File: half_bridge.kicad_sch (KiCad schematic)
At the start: 2 parts, among them U1 74HC04, U2 74HC08

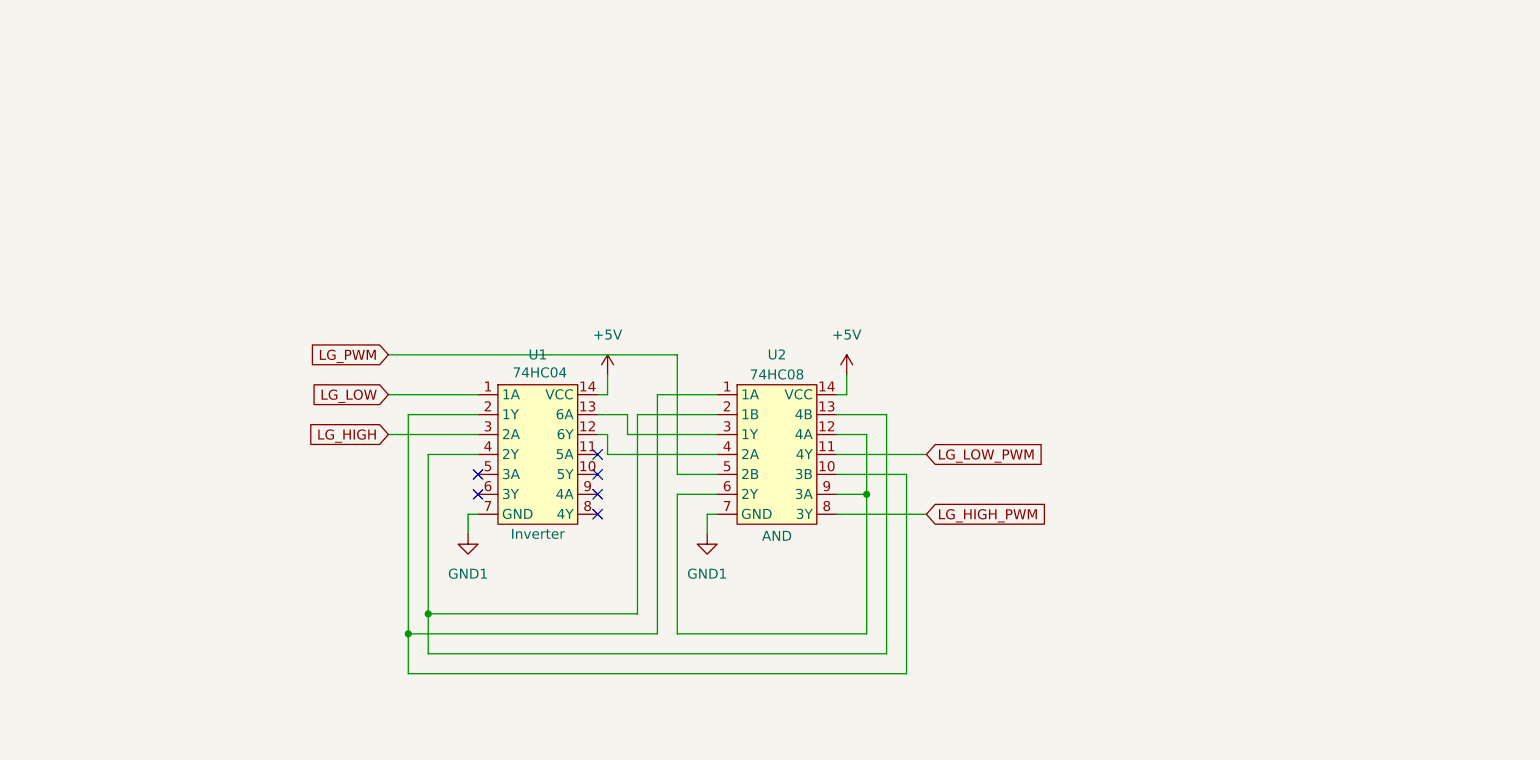
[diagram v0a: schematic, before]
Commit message: Added pwm optocoupler
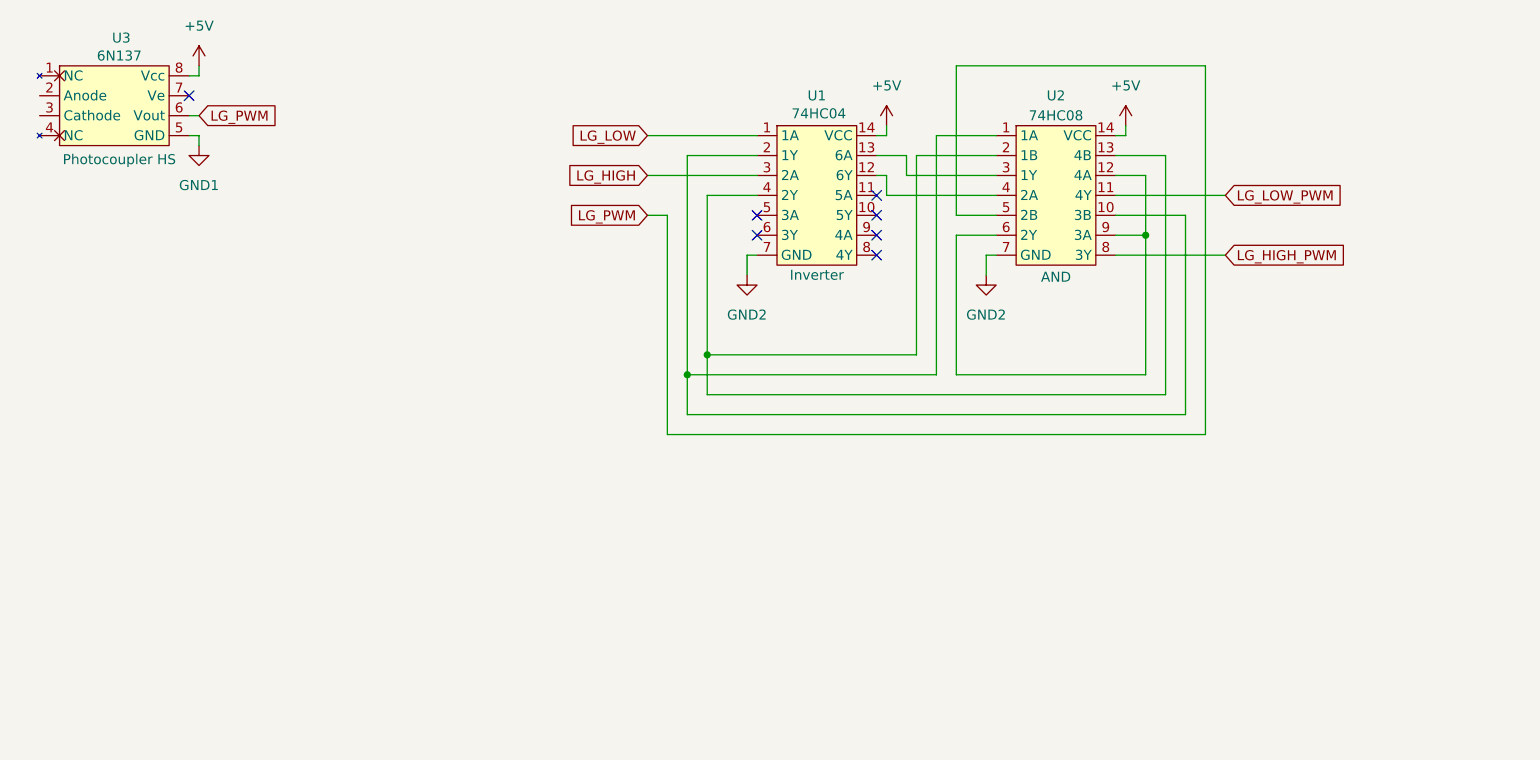
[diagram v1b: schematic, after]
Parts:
- added U3: 6N137, Package_SO:SOP-8_6.605x9.655mm_P2.54mm, symbol symbols:6N137
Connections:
- net +5V: now also U3.8 (Vcc)
- net GND1: now also U3.5 (GND); no longer U1.7 (GND), U2.7 (GND)
- net LG_PWM: now also U3.6 (Vout)
- new net GND2: U1.7 (GND), U2.7 (GND)
- no-connect marks 6 -> 7
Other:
- moved on the sheet: U1, U2

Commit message: Finished logic gates and optocoupler logical connections
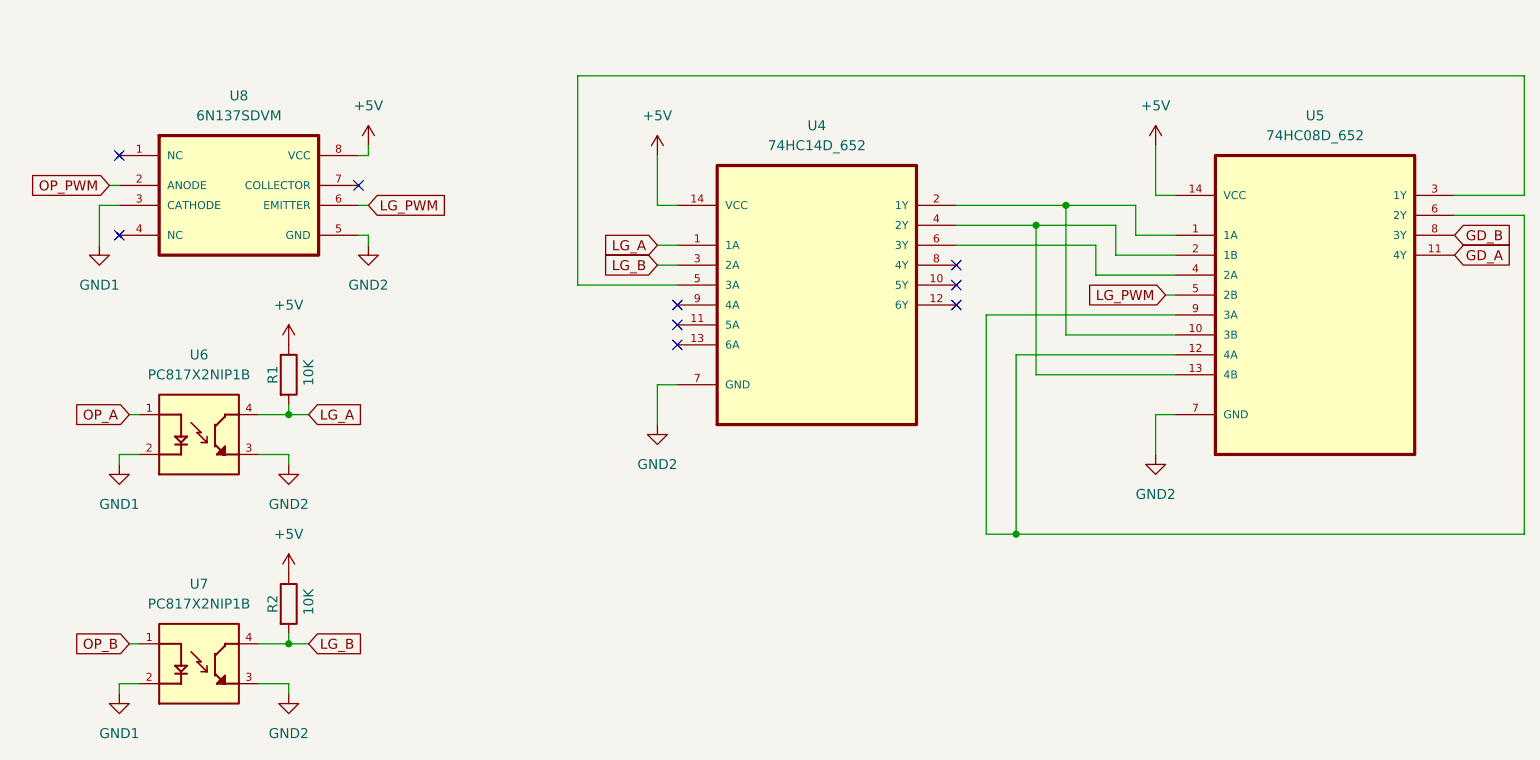
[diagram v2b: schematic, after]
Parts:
- removed U1: 74HC04, Package_SO:SOIC-14_3.9x8.7mm_P1.27mm, symbol symbols:74HC04
- removed U2: 74HC08, Package_SO:SOIC-14_3.9x8.7mm_P1.27mm, symbol symbols:74HC08
- removed U3: 6N137, Package_SO:SOP-8_6.605x9.655mm_P2.54mm, symbol symbols:6N137
- added R1, R2: 10K, footprints:R_0603_1608Metric_Pad0.98x0.95mm_HandSolder, symbol symbols:R_10K_Ohm
- added U4: 74HC14D_652, footprints:SOIC127P600X175-14N, symbol symbols:74HC14D_652
- added U5: 74HC08D_652, footprints:SOIC127P600X175-14N, symbol symbols:74HC08D_652
- added U6, U7: PC817X2NIP1B, footprints:SOIC254P960X420-4N, symbol symbols:PC817X2NIP1B
- added U8: 6N137SDVM, footprints:COUPL_6N138SDM, symbol symbols:6N137SDVM
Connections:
- net +5V: now also R1.1, R2.1, U4.14 (VCC), U5.14 (VCC), U8.8 (VCC)
- net GND1: now also U6.2, U7.2, U8.3 (CATHODE)
- net GND2: now also U4.7 (GND), U5.7 (GND), U6.3, U7.3, U8.5 (GND)
- net LG_PWM: now also U5.5 (2B), U8.6 (EMITTER)
- new net: U4.2 (1Y), U5.1 (1A), U5.10 (3B)
- new net: U4.4 (2Y), U5.13 (4B), U5.2 (1B)
- new net: U4.5 (3A), U5.3 (1Y)
- new net: U4.6 (3Y), U5.4 (2A)
- new net: U5.12 (4A), U5.6 (2Y), U5.9 (3A)
- new net GD_A: U5.11 (4Y)
- new net GD_B: U5.8 (3Y)
- new net LG_A: R1.2, U4.1 (1A), U6.4
- new net LG_B: R2.2, U4.3 (2A), U7.4
- new net OP_A: U6.1
- new net OP_B: U7.1
- new net OP_PWM: U8.2 (ANODE)
- no-connect marks 7 -> 9
